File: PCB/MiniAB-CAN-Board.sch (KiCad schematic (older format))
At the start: 118 parts, among them IC1 ADXL345, J1 105450-0101, J10 TH0, J11 EMOT, J2 CAN, J3 PRB, J4 YES, J5 XES, J6 H0, J7 HEF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

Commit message: Updates to PCB
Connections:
- net +24V: now also JP3.3 (B), JP4.1 (A); no longer JP3.1 (A), JP4.3 (B)
- net +3V3: now also R9.2; no longer R9.1
- net +5V: now also JP3.1 (A), JP4.3 (B); no longer JP3.3 (B), JP4.1 (A)
- net USBDM: no longer R9.2
- net USBDP: now also R9.1
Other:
- moved on the sheet: R9
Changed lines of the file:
@@
 L power:+24V #PWR055
 U 1 1 61951607
-P 6900 2100
-F 0 "#PWR055" H 6900 1950 50  0001 C CNN
-F 1 "+24V" V 6900 2200 50  0000 L CNN
-F 2 "" H 6900 2100 50  0001 C CNN
-F 3 "" H 6900 2100 50  0001 C CNN
-	1    6900 2100
+P 6900 2500
+F 0 "#PWR055" H 6900 2350 50  0001 C CNN
+F 1 "+24V" V 6900 2600 50  0000 L CNN
+F 2 "" H 6900 2500 50  0001 C CNN
+F 3 "" H 6900 2500 50  0001 C CNN
+	1    6900 2500
 	0    1    1    0
 $EndComp
@@
 L power:+5V #PWR057
 U 1 1 61A14721
-P 6900 3600
-F 0 "#PWR057" H 6900 3450 50  0001 C CNN
-F 1 "+5V" V 6900 3700 50  0000 L CNN
-F 2 "" H 6900 3600 50  0001 C CNN
-F 3 "" H 6900 3600 50  0001 C CNN
-	1    6900 3600
+P 6900 4000
+F 0 "#PWR057" H 6900 3850 50  0001 C CNN
+F 1 "+5V" V 6900 4100 50  0000 L CNN
+F 2 "" H 6900 4000 50  0001 C CNN
+F 3 "" H 6900 4000 50  0001 C CNN
+	1    6900 4000
 	0    1    1    0
 $EndComp
@@
 U 1 1 61BD0333
 P 5200 6950
-F 0 "L2" V 5450 6950 50  0000 C CNN
-F 1 "10uH/max. 145mOhm 2A" V 5350 6600 50  0000 C CNN
+F 0 "L2" V 5450 6900 50  0000 C CNN
+F 1 "10uH/max. 145mOhm 2A" V 5350 6500 50  0000 C CNN
 F 2 "Inductor_SMD:L_Sunlord_MWSA0518_5.4x5.2mm" H 5200 6950 50  0001 C CNN
 F 3 "~" H 5200 6950 50  0001 C CNN
@@
 L power:+24V #PWR058
 U 1 1 6237A69C
-P 6900 4000
-F 0 "#PWR058" H 6900 3850 50  0001 C CNN
-F 1 "+24V" V 6900 4100 50  0000 L CNN
-F 2 "" H 6900 4000 50  0001 C CNN
-F 3 "" H 6900 4000 50  0001 C CNN
-	1    6900 4000
+P 6900 3600
+F 0 "#PWR058" H 6900 3450 50  0001 C CNN
+F 1 "+24V" V 6900 3700 50  0000 L CNN
+F 2 "" H 6900 3600 50  0001 C CNN
+F 3 "" H 6900 3600 50  0001 C CNN
+	1    6900 3600
 	0    1    1    0
 $EndComp
@@
 L power:+5V #PWR056
 U 1 1 623AD2A3
-P 6900 2500
-F 0 "#PWR056" H 6900 2350 50  0001 C CNN
-F 1 "+5V" V 6900 2600 50  0000 L CNN
-F 2 "" H 6900 2500 50  0001 C CNN
-F 3 "" H 6900 2500 50  0001 C CNN
-	1    6900 2500
+P 6900 2100
+F 0 "#PWR056" H 6900 1950 50  0001 C CNN
+F 1 "+5V" V 6900 2200 50  0000 L CNN
+F 2 "" H 6900 2100 50  0001 C CNN
+F 3 "" H 6900 2100 50  0001 C CNN
+	1    6900 2100
 	0    1    1    0
 $EndComp
@@
 Wire Wire Line
 	2150 5400 2250 5400
-Wire Wire Line
-	2450 5500 2450 5650
 $Comp
 L Device:R_Small R7
@@
 Wire Wire Line
 	2150 5500 2250 5500
-$Comp
-L Device:R_Small R9
-U 1 1 62E11560
-P 2450 5750
-F 0 "R9" V 2550 5800 50  0000 C CNN
-F 1 "2.2k" V 2350 5750 50  0000 C CNN
-F 2 "Resistor_SMD:R_0402_1005Metric" H 2450 5750 50  0001 C CNN
-F 3 "~" H 2450 5750 50  0001 C CNN
-	1    2450 5750
-	-1   0    0    1
-$EndComp
-$Comp
-L power:+3V3 #PWR015
-U 1 1 62E11CD8
-P 2450 5850
-F 0 "#PWR015" H 2450 5700 50  0001 C CNN
-F 1 "+3V3" V 2450 5950 50  0000 L CNN
-F 2 "" H 2450 5850 50  0001 C CNN
-F 3 "" H 2450 5850 50  0001 C CNN
-	1    2450 5850
-	-1   0    0    1
-$EndComp
 $Comp
 L Device:R_Small R1
@@
 	1    0    0    -1
 $EndComp
-Connection ~ 2450 5500
 Wire Wire Line
 	2450 5500 2650 5500
@@
 Wire Wire Line
 	2650 5500 2650 5550
+Connection ~ 2450 5400
+$Comp
+L power:+3V3 #PWR015
+U 1 1 62E11CD8
+P 2450 4900
+F 0 "#PWR015" H 2450 4750 50  0001 C CNN
+F 1 "+3V3" V 2450 5000 50  0000 L CNN
+F 2 "" H 2450 4900 50  0001 C CNN
+F 3 "" H 2450 4900 50  0001 C CNN
+	1    2450 4900
+	1    0    0    -1
+$EndComp
+$Comp
+L Device:R_Small R9
+U 1 1 62E11560
+P 2450 5000
+F 0 "R9" V 2550 5050 50  0000 C CNN
+F 1 "2.2k" V 2350 5000 50  0000 C CNN
+F 2 "Resistor_SMD:R_0402_1005Metric" H 2450 5000 50  0001 C CNN
+F 3 "~" H 2450 5000 50  0001 C CNN
+	1    2450 5000
+	-1   0    0    1
+$EndComp
+Wire Wire Line
+	2450 5100 2450 5400
 $EndSCHEMATC

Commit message: add debug port and rework of schematic
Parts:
- added C?: 0.1uF, Capacitor_SMD:C_0402_1005Metric, symbol Device:C_Small
- added J?: DBG, symbol Connector_Generic:Conn_02x03_Odd_Even
- added R? (x2): 10k, Resistor_SMD:R_0402_1005Metric, symbol Device:R_Small
- added TP? (x4): TestPoint, symbol Connector:TestPoint
- J11: value EMOT -> STEPPER
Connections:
- net +24V: now also TP?.1
- net +3V3: now also C?.1, J?.2 (Pin_2), TP?.1
- net BOOT0: now also TP?.1
- net BOOT1: now also J?.1 (Pin_1)
- net GND: now also C?.2, J?.4 (Pin_4), R?.1, R?.1, TP?.1
- net NRST: now also J?.3 (Pin_3)
- net SWCLK: now also J?.6 (Pin_6), R?.2
- net SWDIO: now also J?.5 (Pin_5), R?.2
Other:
- note added: "3.3V"
- note added: "5V Regulator"
- note added: "ADXL"
- note added: "Alt:\nTPS54308\nTPS54302"
- note added: "CAN"
- note added: "Debug"
- note added: "Endstops"
- note added: "Heater"
- note added: "Heater Fan"
- note added: "MCU"
- note added: "Part Cooling Fan"
- note added: "Stepper Driver"
- note added: "Test Points"
- note added: "Thermistors"
- note added: "USB"
- moved on the sheet: C13, C15, C20, C21, C23, C24, C25, C26, C27, C28, C29, C30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

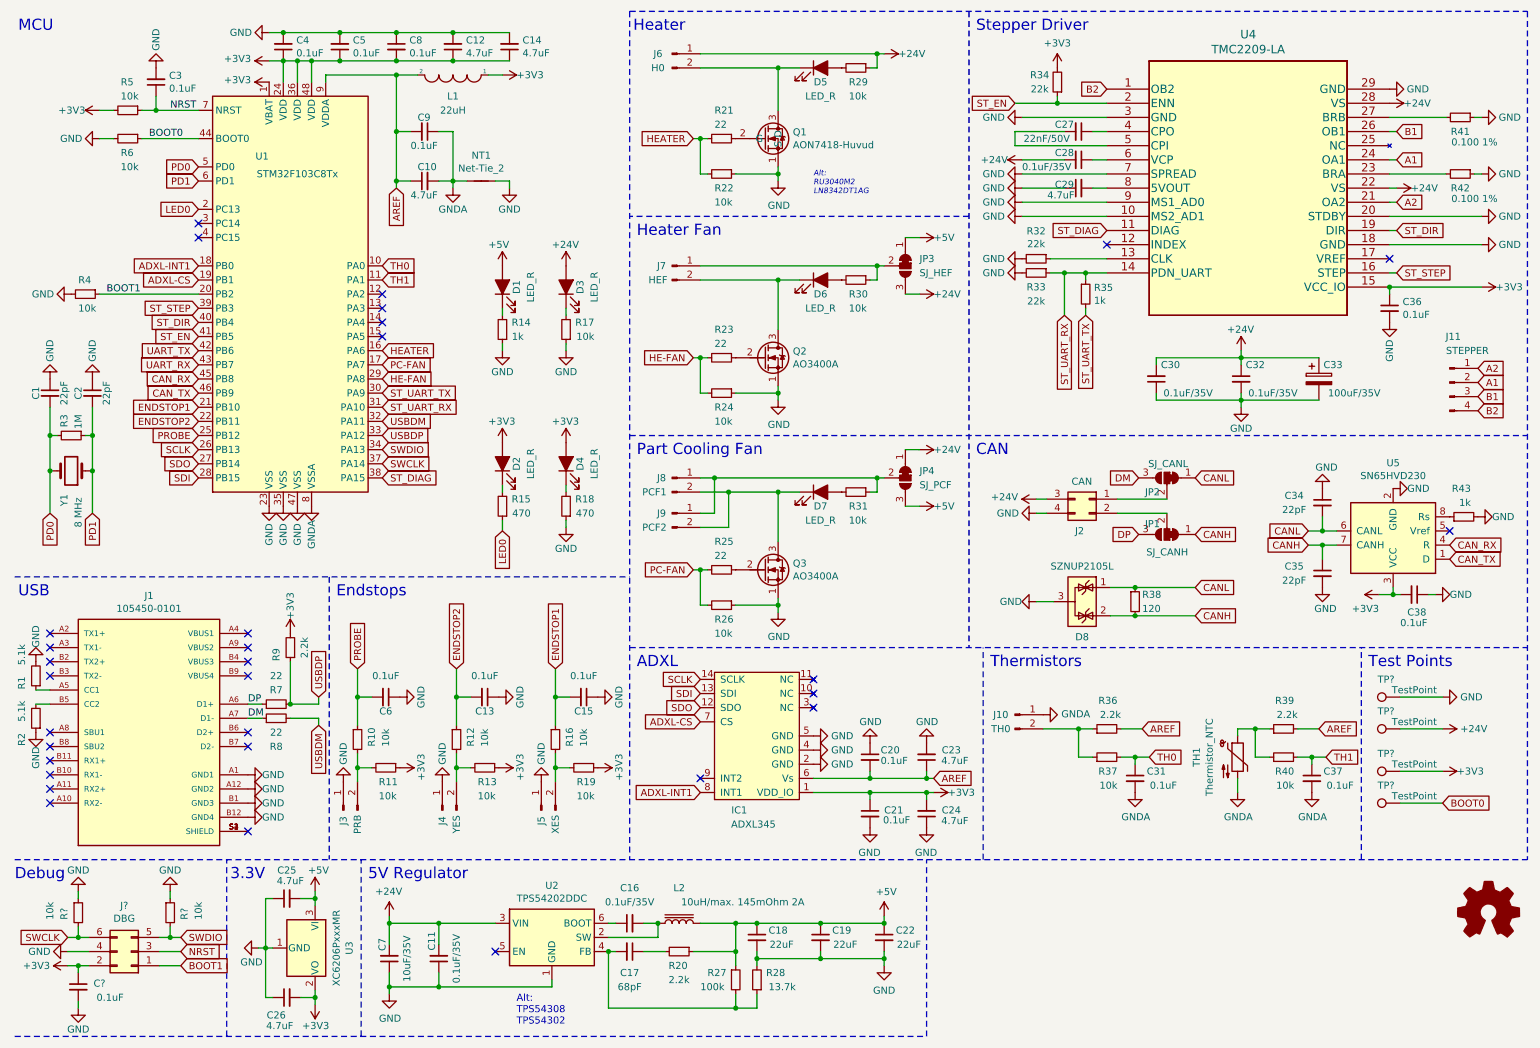
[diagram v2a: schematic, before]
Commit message: Add 3 Pin Endstops + LED Port
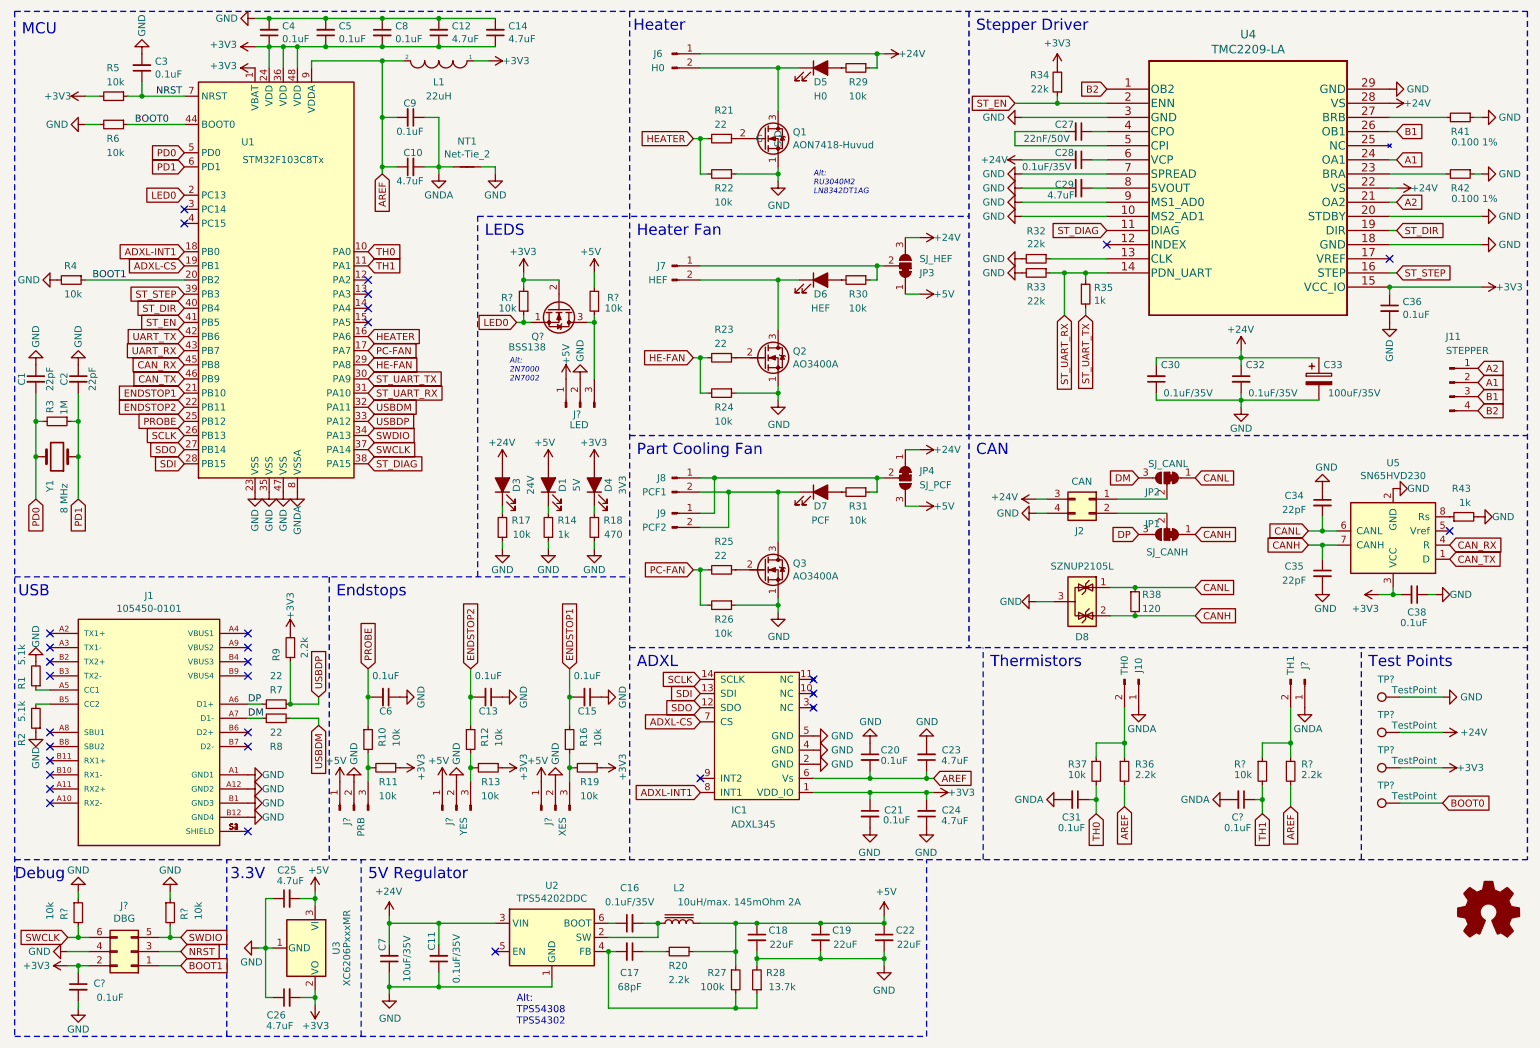
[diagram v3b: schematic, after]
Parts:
- removed C37: 0.1uF, Capacitor_SMD:C_0402_1005Metric, symbol Device:C_Small
- removed D2: LED_R, LED_SMD:LED_0402_1005Metric, symbol Device:LED_ALT
- removed J3: PRB, Connector_JST:JST_PH_B2B-PH-K_1x02_P2.00mm_Vertical, symbol Connector:Conn_01x02_Male
- removed J4: YES, Connector_JST:JST_PH_B2B-PH-K_1x02_P2.00mm_Vertical, symbol Connector:Conn_01x02_Male
- removed J5: XES, Connector_JST:JST_PH_B2B-PH-K_1x02_P2.00mm_Vertical, symbol Connector:Conn_01x02_Male
- removed R15: 470, Resistor_SMD:R_0402_1005Metric, symbol Device:R_Small
- removed R39: 2.2k, Resistor_SMD:R_0402_1005Metric, symbol Device:R_Small
- removed R40: 10k, Resistor_SMD:R_0402_1005Metric, symbol Device:R_Small
- removed TH1: Thermistor_NTC, Resistor_SMD:R_0603_1608Metric, symbol Device:Thermistor_NTC
- added C?: 0.1uF, Capacitor_SMD:C_0402_1005Metric, symbol Device:C_Small
- added J?: PRB, symbol Connector:Conn_01x03_Male
- added J?: YES, symbol Connector:Conn_01x03_Male
- added J?: XES, symbol Connector:Conn_01x03_Male
- added J?: LED, symbol Connector:Conn_01x03_Male
- added J?: TH1, Connector_JST:JST_PH_B2B-PH-K_1x02_P2.00mm_Vertical, symbol Connector:Conn_01x02_Male
- added Q?: BSS138, Package_TO_SOT_THT:TO-92_Inline, symbol Transistor_FET:2N7000
- added R? (x3): 10k, Resistor_SMD:R_0402_1005Metric, symbol Device:R_Small
- added R?: 2.2k, Resistor_SMD:R_0402_1005Metric, symbol Device:R_Small
- D1: value LED_R -> 5V
- D3: value LED_R -> 24V
- D4: value LED_R -> 3V3
- D5: value LED_R -> H0
- D6: value LED_R -> HEF
- D7: value LED_R -> PCF
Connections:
- net +3V3: now also Q?.2 (G), R?.2
- net +5V: now also J?.1 (Pin_1), J?.1 (Pin_1), J?.1 (Pin_1), J?.1 (Pin_1), R?.2
- net AREF: now also R?.2
- net GND: now also J?.2 (Pin_2), J?.2 (Pin_2), J?.2 (Pin_2), J?.2 (Pin_2)
- net GNDA: now also C?.2, J?.1 (Pin_1)
- net LED0: now also Q?.1 (S), R?.1
- net TH1: now also C?.1, R?.2
- net at R16.2, R19.2: now also J?.3 (Pin_3)
- net at R12.2, R13.2: now also J?.3 (Pin_3)
- net at R10.2, R11.2: now also J?.3 (Pin_3)
- new net: J?.3 (Pin_3), Q?.3 (D), R?.1
- new net: J?.2 (Pin_2), R?.1, R?.1
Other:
- note added: "Alt:\n2N7000\n2N7002"
- note added: "LEDS\n"
- moved on the sheet: C1, C10, C12, C13, C14, C15, C2, C3, C31, C4, C5, C8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

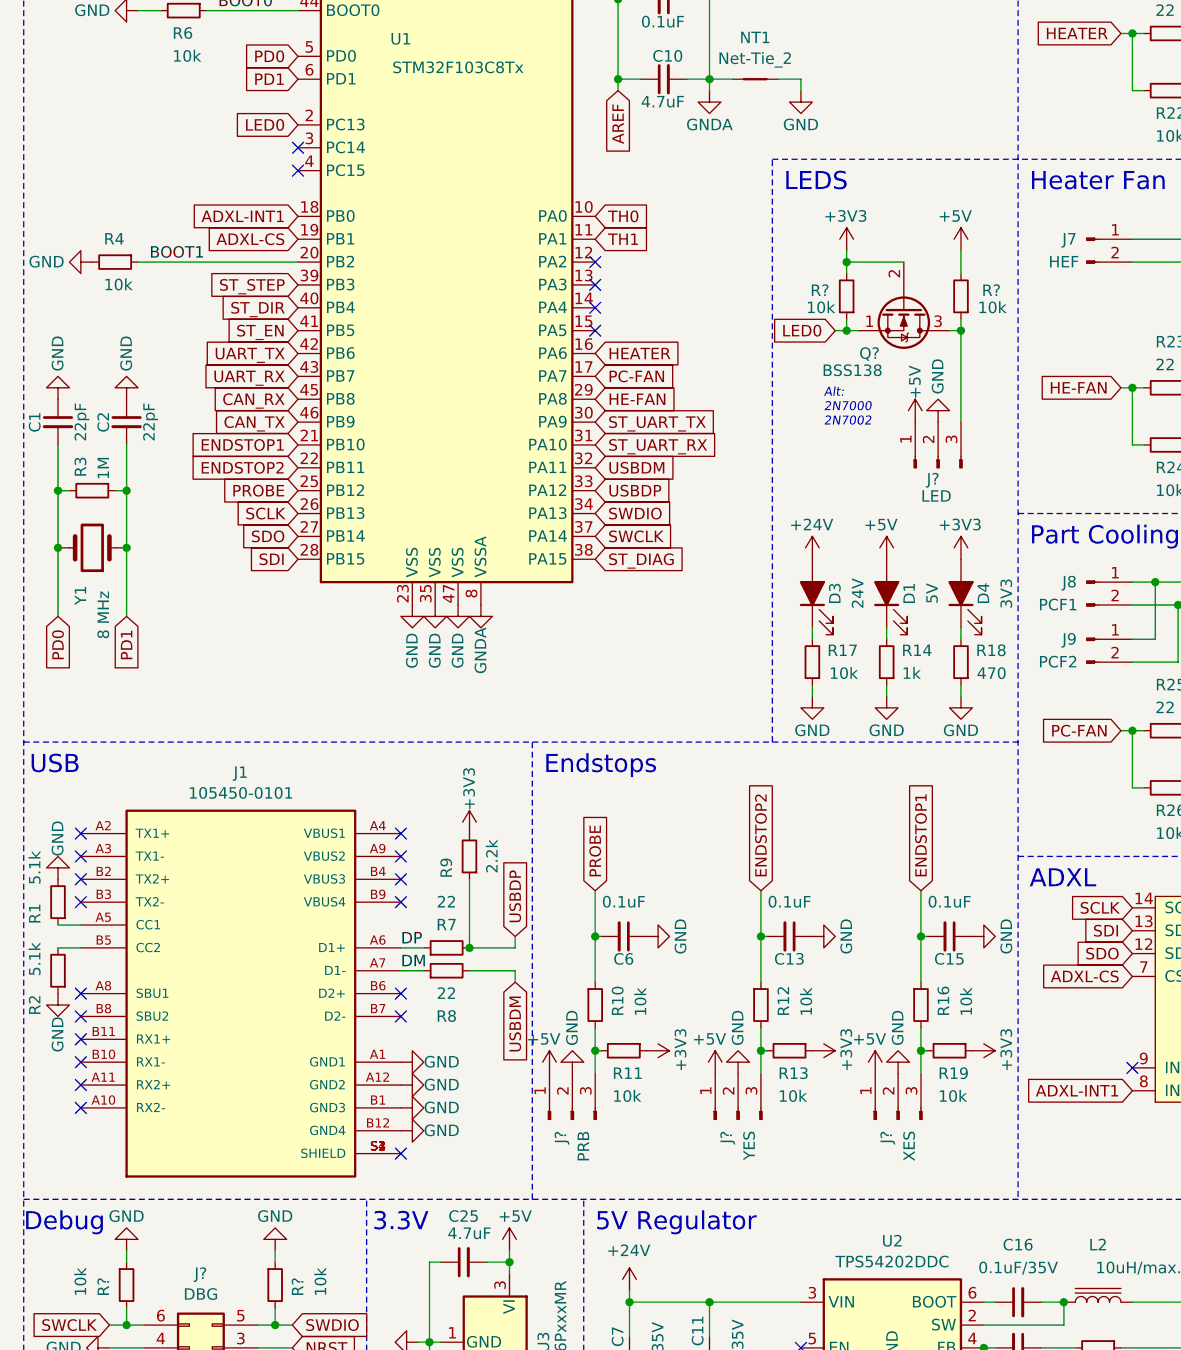
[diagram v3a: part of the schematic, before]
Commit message: change rgb led pin order, some rearrangements
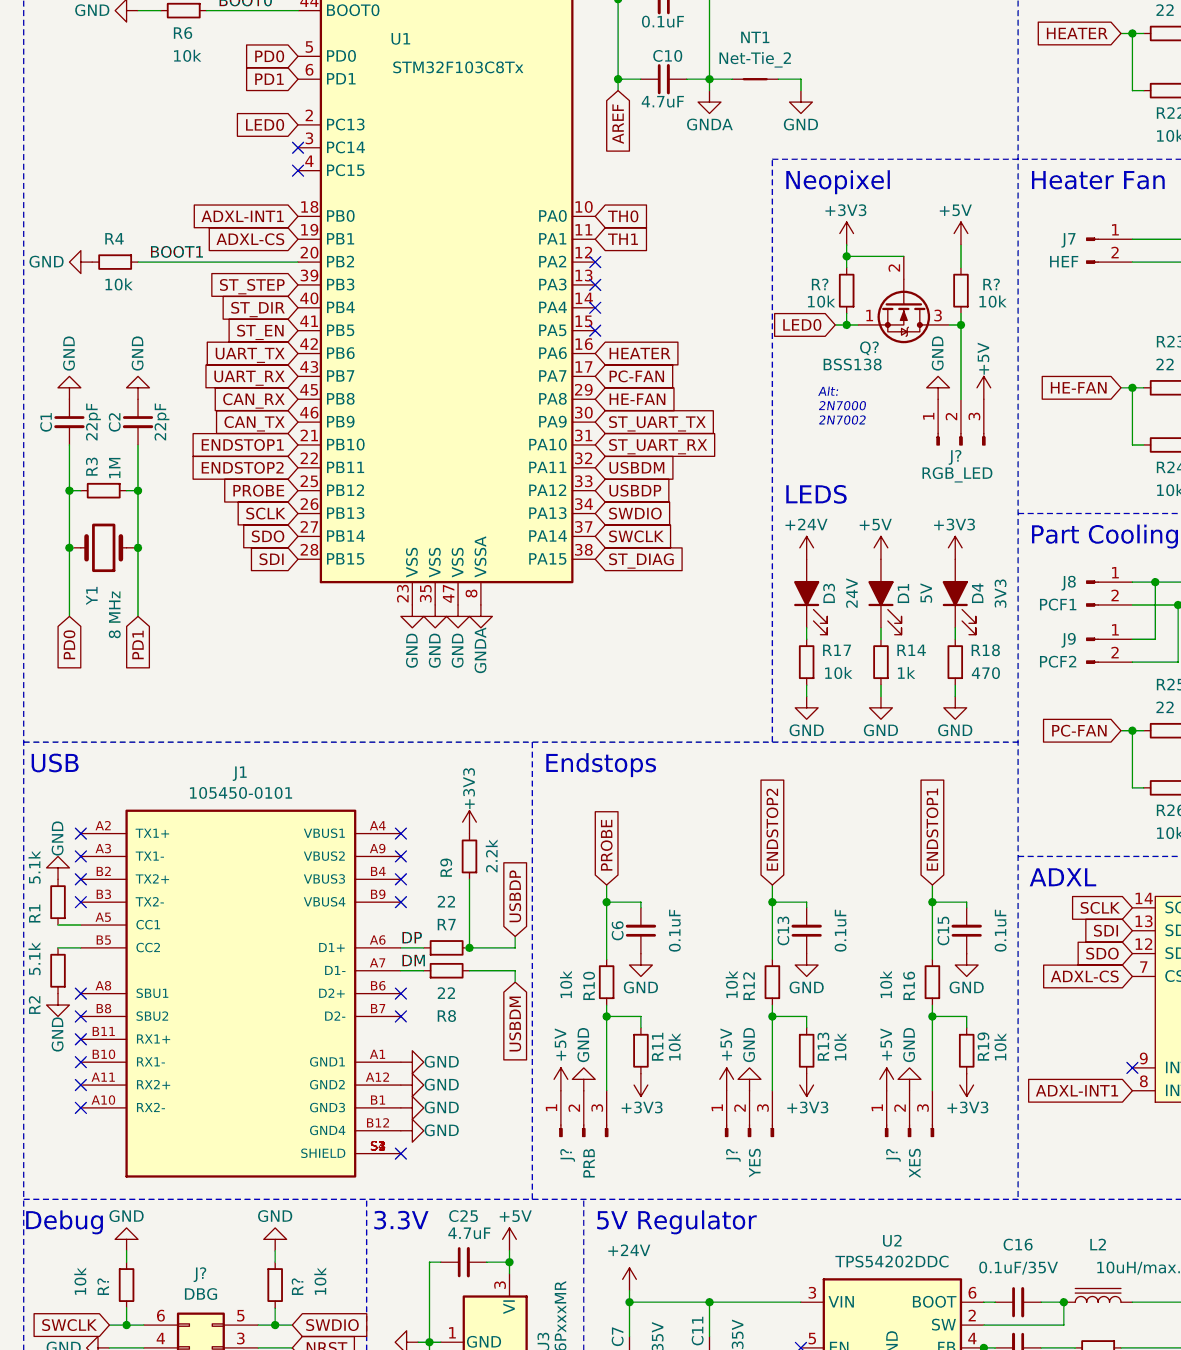
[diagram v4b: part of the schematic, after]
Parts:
- J?: value LED -> RGB_LED
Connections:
- net +3V3: now also R11.2, R13.2, R19.2; no longer R11.1, R13.1, R19.1
- net +5V: now also J?.3 (Pin_3); no longer J?.1 (Pin_1)
- net ENDSTOP1: now also R16.2; no longer R16.1
- net ENDSTOP2: now also R12.2; no longer R12.1
- net GND: now also J?.1 (Pin_1); no longer J?.2 (Pin_2)
- net PROBE: now also R10.2; no longer R10.1
- net at Q?.3 (D), R?.1: now also J?.2 (Pin_2); no longer J?.3 (Pin_3)
- new net: J?.3 (Pin_3), R10.1, R11.1
- new net: J?.3 (Pin_3), R12.1, R13.1
- new net: J?.3 (Pin_3), R16.1, R19.1
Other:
- note added: "Neopixel"
- moved on the sheet: C1, C13, C15, C2, C6, D1, D3, D4, J?, Q?, R10, R11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

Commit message: add missing footprints
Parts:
- J12: renamed from J?; footprint (none) -> Connector_PinHeader_1.27mm:PinHeader_2x03_P1.27mm_Vertical_SMD
- J13, J3, J4, J5: renamed from J?; footprint (none) -> Connector_JST:JST_PH_B3B-PH-K_1x03_P2.00mm_Vertical
- Q4: renamed from Q?; footprint Package_TO_SOT_THT:TO-92_Inline -> Package_TO_SOT_SMD:SOT-23
- TP1, TP2, TP3, TP4: renamed from TP?; footprint (none) -> TestPoint:TestPoint_Pad_D1.5mm
- gave numbers to parts that had none: 9
